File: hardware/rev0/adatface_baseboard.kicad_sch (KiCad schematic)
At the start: 89 parts, among them J1 Conn_01x06_Male, J2 Conn_02x32_Odd_Even, J3 Conn_02x32_Odd_Even, J4 Connector_USB_C_Receptacle_US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, J5 Connector_USB_C_Receptacle_US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, J6 Conn_01x06_Male, J7 Conn_01x23_Male, J8 Conn_01x01_Male, J9 Conn_01x01_Male, U1 PLR135-T10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

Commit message: Fix bugs in rev0
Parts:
- removed J7: Conn_01x23_Male, Connector_PinHeader_2.54mm:PinHeader_1x23_P2.54mm_Vertical, symbol Connector:Conn_01x23_Male
- added J7: Conn_01x26_Male, Connector_PinHeader_2.54mm:PinHeader_1x26_P2.54mm_Horizontal, symbol Connector:Conn_01x26_Male
- J8, J9: footprint Connector_PinHeader_2.54mm:PinHeader_1x01_P2.54mm_Vertical -> Connector_PinHeader_2.54mm:PinHeader_1x01_P2.54mm_Horizontal
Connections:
- net +3V3: now also J7.2 (Pin_2)
- net GND: now also J7.1 (Pin_1), J7.3 (Pin_3)
- net at J2.8 (Pin_8): now also J7.4 (Pin_4)
- net at J2.26 (Pin_26): now also J7.13 (Pin_13)
- net at J2.28 (Pin_28): now also J7.14 (Pin_14)
- net at J2.30 (Pin_30): now also J7.15 (Pin_15)
- net at J2.32 (Pin_32): now also J7.16 (Pin_16)
- net at J2.34 (Pin_34): now also J7.17 (Pin_17)
- net at J2.36 (Pin_36): now also J7.18 (Pin_18)
- net at J2.38 (Pin_38): now also J7.19 (Pin_19)
- net at J2.40 (Pin_40): now also J7.20 (Pin_20)
- net at J2.42 (Pin_42): now also J7.21 (Pin_21)
- net at J2.44 (Pin_44): now also J7.22 (Pin_22)
- net at J2.10 (Pin_10): now also J7.5 (Pin_5)
- net at J2.46 (Pin_46): now also J7.23 (Pin_23)
- net at J2.48 (Pin_48): now also J7.24 (Pin_24)
- net at J2.50 (Pin_50): now also J7.25 (Pin_25)
- net at J2.52 (Pin_52): now also J7.26 (Pin_26)
- net at J2.12 (Pin_12): now also J7.6 (Pin_6)
- net at J2.14 (Pin_14): now also J7.7 (Pin_7)
- net at J2.16 (Pin_16): now also J7.8 (Pin_8)
- net at J2.18 (Pin_18): now also J7.9 (Pin_9)
- net at J2.20 (Pin_20): now also J7.10 (Pin_10)
- net at J2.22 (Pin_22): now also J7.11 (Pin_11)
- net at J2.24 (Pin_24): now also J7.12 (Pin_12)

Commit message: Fix missing symbol and footprint libraries for toslink
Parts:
- TR1, TR2, TR3, TR4: footprint XDCR_PLT133/T10W -> toslink:PLT133_T10W; symbol PLT133_T10W:PLT133_T10W -> toslink:PLT133_T10W
- U1, U2, U3, U4: footprint PLR135-T10_PLT133-T10W -> toslink:PLR135-T10_PLT133-T10W; symbol PLR135_T10:PLR135-T10 -> toslink:PLR135_T10
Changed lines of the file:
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@@
     (pin "1")
   )
-  (symbol (lib_id "PLT133_T10W:PLT133_T10W") (at 82.55 147.32 0) (unit 1)
+  (symbol (lib_id "toslink:PLT133_T10W") (at 82.55 147.32 0) (unit 1)
     (in_bom yes) (on_board yes) (fields_autoplaced)
     (property "Reference" "TR4" (id 0) (at 82.55 135.7334 0))
     (property "Value" "PLT133_T10W" (id 1) (at 82.55 138.5085 0))
-    (property "Footprint" "XDCR_PLT133/T10W" (id 2) (at 82.55 147.32 0)
+    (property "Footprint" "toslink:PLT133_T10W" (id 2) (at 82.55 147.32 0)
       (effects (font (size 1.27 1.27)) (justify left bottom) hide)
     )
@@
     (pin "2")
   )
-  (symbol (lib_id "PLR135_T10:PLR135-T10") (at 83.82 63.5 0) (unit 1)
+  (symbol (lib_id "toslink:PLR135_T10") (at 83.82 63.5 0) (unit 1)
     (in_bom yes) (on_board yes) (fields_autoplaced)
     (property "Reference" "U2" (id 0) (at 93.8785 62.5915 0)
@@
       (effects (font (size 1.27 1.27)) (justify left))
     )
-    (property "Footprint" "PLR135-T10_PLT133-T10W" (id 2) (at 83.82 63.5 0)
+    (property "Footprint" "toslink:PLR135-T10_PLT133-T10W" (id 2) (at 83.82 63.5 0)
       (effects (font (size 1.27 1.27)) (justify left bottom) hide)
     )
@@
     (pin "1")
   )
-  (symbol (lib_id "PLR135_T10:PLR135-T10") (at 83.82 119.38 0) (unit 1)
+  (symbol (lib_id "toslink:PLR135_T10") (at 83.82 119.38 0) (unit 1)
     (in_bom yes) (on_board yes) (fields_autoplaced)
     (property "Reference" "U3" (id 0) (at 93.8785 118.4715 0)
@@
       (effects (font (size 1.27 1.27)) (justify left))
     )
-    (property "Footprint" "PLR135-T10_PLT133-T10W" (id 2) (at 83.82 119.38 0)
+    (property "Footprint" "toslink:PLR135-T10_PLT133-T10W" (id 2) (at 83.82 119.38 0)
       (effects (font (size 1.27 1.27)) (justify left bottom) hide)
     )
@@
     (pin "1")
   )
-  (symbol (lib_id "PLT133_T10W:PLT133_T10W") (at 82.55 91.44 0) (unit 1)
+  (symbol (lib_id "toslink:PLT133_T10W") (at 82.55 91.44 0) (unit 1)
     (in_bom yes) (on_board yes) (fields_autoplaced)
     (property "Reference" "TR3" (id 0) (at 82.55 79.8534 0))
     (property "Value" "PLT133_T10W" (id 1) (at 82.55 82.6285 0))
-    (property "Footprint" "XDCR_PLT133/T10W" (id 2) (at 82.55 91.44 0)
+    (property "Footprint" "toslink:PLT133_T10W" (id 2) (at 82.55 91.44 0)
       (effects (font (size 1.27 1.27)) (justify left bottom) hide)
     )
@@
     (pin "1")
   )
-  (symbol (lib_id "PLT133_T10W:PLT133_T10W") (at 82.55 35.56 0) (unit 1)
+  (symbol (lib_id "toslink:PLT133_T10W") (at 82.55 35.56 0) (unit 1)
     (in_bom yes) (on_board yes) (fields_autoplaced)
     (property "Reference" "TR2" (id 0) (at 82.55 23.9734 0))
     (property "Value" "PLT133_T10W" (id 1) (at 82.55 26.7485 0))
-    (property "Footprint" "XDCR_PLT133/T10W" (id 2) (at 82.55 35.56 0)
+    (property "Footprint" "toslink:PLT133_T10W" (id 2) (at 82.55 35.56 0)
       (effects (font (size 1.27 1.27)) (justify left bottom) hide)
     )
@@
     (pin "5")
   )
-  (symbol (lib_id "PLR135_T10:PLR135-T10") (at 82.55 232.41 0) (unit 1)
+  (symbol (lib_id "toslink:PLR135_T10") (at 82.55 232.41 0) (unit 1)
     (in_bom yes) (on_board yes) (fields_autoplaced)
     (property "Reference" "U1" (id 0) (at 92.6085 231.5015 0)
@@
       (effects (font (size 1.27 1.27)) (justify left))
     )
-    (property "Footprint" "PLR135-T10_PLT133-T10W" (id 2) (at 82.55 232.41 0)
+    (property "Footprint" "toslink:PLR135-T10_PLT133-T10W" (id 2) (at 82.55 232.41 0)
       (effects (font (size 1.27 1.27)) (justify left bottom) hide)
     )
@@
     (pin "1")
   )
-  (symbol (lib_id "PLT133_T10W:PLT133_T10W") (at 81.28 204.47 0) (unit 1)
+  (symbol (lib_id "toslink:PLT133_T10W") (at 81.28 204.47 0) (unit 1)
     (in_bom yes) (on_board yes) (fields_autoplaced)
     (property "Reference" "TR1" (id 0) (at 81.28 192.8834 0))
     (property "Value" "PLT133_T10W" (id 1) (at 81.28 195.6585 0))
-    (property "Footprint" "XDCR_PLT133/T10W" (id 2) (at 82.55 191.77 0)
+    (property "Footprint" "toslink:PLT133_T10W" (id 2) (at 81.28 204.47 0)
       (effects (font (size 1.27 1.27)) (justify left bottom) hide)
     )
@@
       (effects (font (size 1.27 1.27)) (justify left bottom) hide)
     )
-    (property "MAXIMUM_PACKAGE_HEIGHT" "10.3 mm" (id 4) (at 87.63 194.31 0)
+    (property "MAXIMUM_PACKAGE_HEIGHT" "10.3 mm" (id 4) (at 81.28 204.47 0)
       (effects (font (size 1.27 1.27)) (justify left bottom) hide)
     )
-    (property "MANUFACTURER" "Everlight Electronics" (id 5) (at 81.28 214.63 0)
+    (property "MANUFACTURER" "Everlight Electronics" (id 5) (at 81.28 204.47 0)
       (effects (font (size 1.27 1.27)) (justify left bottom) hide)
     )
@@
       (effects (font (size 1.27 1.27)) (justify left bottom) hide)
     )
-    (property "STANDARD" "Manufacturer Recommendations" (id 7) (at 80.01 215.9 0)
+    (property "STANDARD" "Manufacturer Recommendations" (id 7) (at 81.28 204.47 0)
       (effects (font (size 1.27 1.27)) (justify left bottom) hide)
     )
@@
     (pin "1")
   )
-  (symbol (lib_id "PLR135_T10:PLR135-T10") (at 83.82 175.26 0) (unit 1)
+  (symbol (lib_id "toslink:PLR135_T10") (at 83.82 175.26 0) (unit 1)
     (in_bom yes) (on_board yes) (fields_autoplaced)
     (property "Reference" "U4" (id 0) (at 93.8785 174.3515 0)
@@
       (effects (font (size 1.27 1.27)) (justify left))
     )
-    (property "Footprint" "PLR135-T10_PLT133-T10W" (id 2) (at 83.82 175.26 0)
+    (property "Footprint" "toslink:PLR135-T10_PLT133-T10W" (id 2) (at 83.82 175.26 0)
       (effects (font (size 1.27 1.27)) (justify left bottom) hide)
     )
@@
     )
     (path "/e305be24-ecd4-4f67-94e9-58c892d869c0"
-      (reference "TR1") (unit 1) (value "PLT133_T10W") (footprint "XDCR_PLT133/T10W")
+      (reference "TR1") (unit 1) (value "PLT133_T10W") (footprint "toslink:PLT133_T10W")
     )
     (path "/d307c6e7-be3d-479f-a065-7e94414e36ef"
-      (reference "TR2") (unit 1) (value "PLT133_T10W") (footprint "XDCR_PLT133/T10W")
+      (reference "TR2") (unit 1) (value "PLT133_T10W") (footprint "toslink:PLT133_T10W")
     )
     (path "/b68d2074-2874-4baf-9fc7-73bd2b8e0725"
-      (reference "TR3") (unit 1) (value "PLT133_T10W") (footprint "XDCR_PLT133/T10W")
+      (reference "TR3") (unit 1) (value "PLT133_T10W") (footprint "toslink:PLT133_T10W")
     )
     (path "/100b613e-a6ff-4d41-9825-5ac37f8b1fa0"
-      (reference "TR4") (unit 1) (value "PLT133_T10W") (footprint "XDCR_PLT133/T10W")
+      (reference "TR4") (unit 1) (value "PLT133_T10W") (footprint "toslink:PLT133_T10W")
     )
     (path "/d44226c0-bd8c-4098-ad30-873ebe731ecc"
-      (reference "U1") (unit 1) (value "PLR135-T10") (footprint "PLR135-T10_PLT133-T10W")
+      (reference "U1") (unit 1) (value "PLR135-T10") (footprint "toslink:PLR135-T10_PLT133-T10W")
     )
     (path "/99f4d10a-336e-460f-ac98-498fefdb9e43"
-      (reference "U2") (unit 1) (value "PLR135-T10") (footprint "PLR135-T10_PLT133-T10W")
+      (reference "U2") (unit 1) (value "PLR135-T10") (footprint "toslink:PLR135-T10_PLT133-T10W")
     )
     (path "/a504528d-b263-479b-914d-740c72f5070c"
-      (reference "U3") (unit 1) (value "PLR135-T10") (footprint "PLR135-T10_PLT133-T10W")
+      (reference "U3") (unit 1) (value "PLR135-T10") (footprint "toslink:PLR135-T10_PLT133-T10W")
     )
     (path "/e97ce483-a060-4946-827f-bc98193607f2"
-      (reference "U4") (unit 1) (value "PLR135-T10") (footprint "PLR135-T10_PLT133-T10W")
+      (reference "U4") (unit 1) (value "PLR135-T10") (footprint "toslink:PLR135-T10_PLT133-T10W")
     )
     (path "/0b1e87ea-f6ed-4224-97ad-09fa0b4bc814"

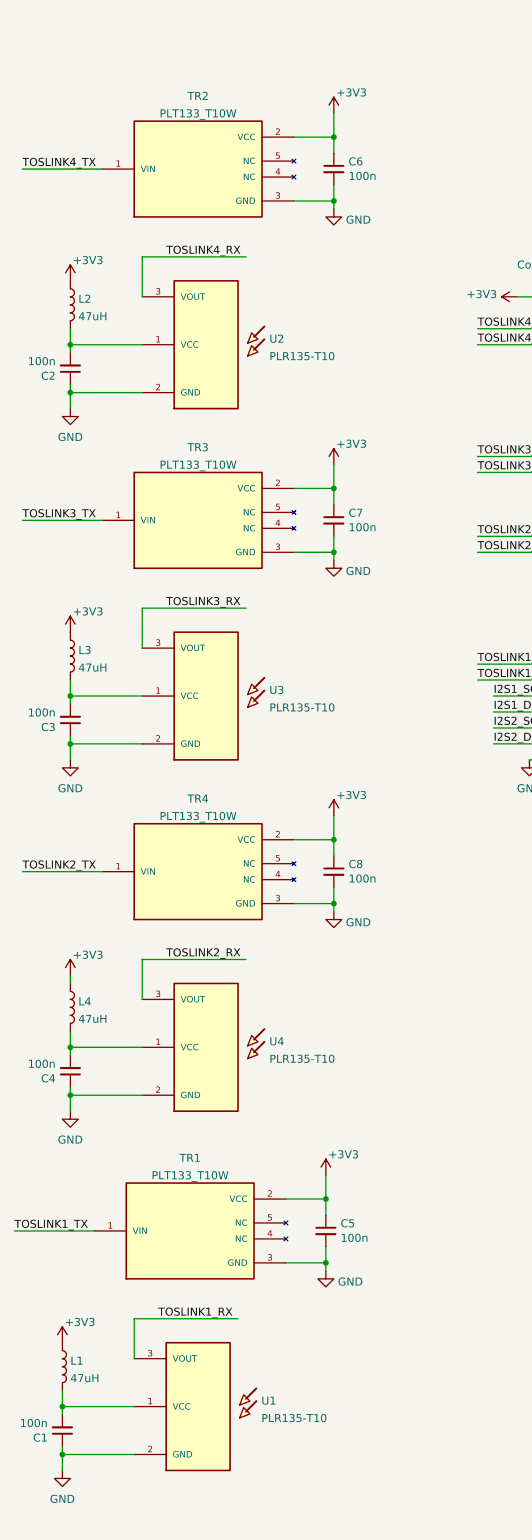
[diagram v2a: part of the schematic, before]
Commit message: change toslink footprints to T8 variation
Footprint is the same except for the edition of NPTH for
plastic mounting feet, so either T8 or T10 versions can
be used.
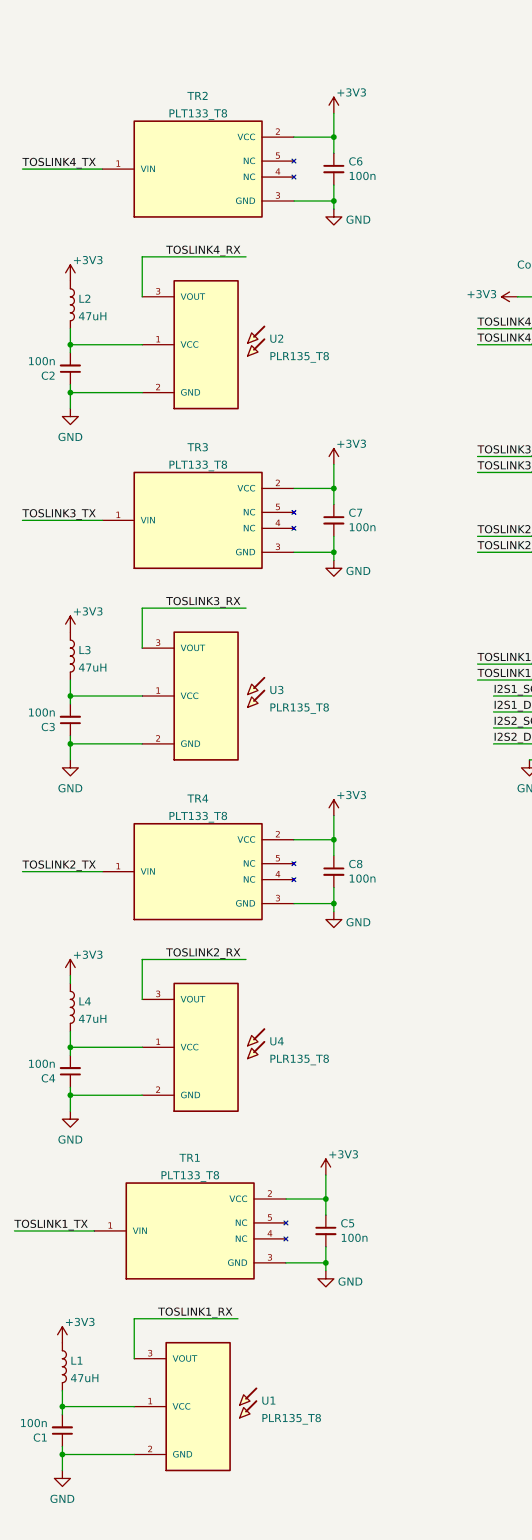
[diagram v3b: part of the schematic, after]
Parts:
- TR1, TR2, TR3, TR4: value PLT133_T10W -> PLT133_T8; footprint toslink:PLT133_T10W -> toslink:PLT133_T8; symbol toslink:PLT133_T10W -> toslink:PLT133_T8
- U1, U2, U3, U4: value PLR135-T10 -> PLR135_T8; footprint toslink:PLR135-T10_PLT133-T10W -> toslink:PLR135-T8_PLT133-T8; symbol toslink:PLR135_T10 -> toslink:PLR135_T8
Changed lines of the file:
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@@
     (pin "1")
   )
-  (symbol (lib_id "toslink:PLT133_T10W") (at 82.55 147.32 0) (unit 1)
+  (symbol (lib_id "toslink:PLT133_T8") (at 82.55 147.32 0) (unit 1)
     (in_bom yes) (on_board yes) (fields_autoplaced)
     (property "Reference" "TR4" (id 0) (at 82.55 135.7334 0))
-    (property "Value" "PLT133_T10W" (id 1) (at 82.55 138.5085 0))
-    (property "Footprint" "toslink:PLT133_T10W" (id 2) (at 82.55 147.32 0)
+    (property "Value" "PLT133_T8" (id 1) (at 82.55 138.5085 0))
+    (property "Footprint" "toslink:PLT133_T8" (id 2) (at 82.55 147.32 0)
       (effects (font (size 1.27 1.27)) (justify left bottom) hide)
     )
@@
     (pin "2")
   )
-  (symbol (lib_id "toslink:PLR135_T10") (at 83.82 63.5 0) (unit 1)
+  (symbol (lib_id "toslink:PLR135_T8") (at 83.82 63.5 0) (unit 1)
     (in_bom yes) (on_board yes) (fields_autoplaced)
     (property "Reference" "U2" (id 0) (at 93.8785 62.5915 0)
       (effects (font (size 1.27 1.27)) (justify left))
     )
-    (property "Value" "PLR135-T10" (id 1) (at 93.8785 65.3666 0)
+    (property "Value" "PLR135_T8" (id 1) (at 93.8785 65.3666 0)
       (effects (font (size 1.27 1.27)) (justify left))
     )
-    (property "Footprint" "toslink:PLR135-T10_PLT133-T10W" (id 2) (at 83.82 63.5 0)
+    (property "Footprint" "toslink:PLR135-T8_PLT133-T8" (id 2) (at 83.82 63.5 0)
       (effects (font (size 1.27 1.27)) (justify left bottom) hide)
     )
@@
     (pin "1")
   )
-  (symbol (lib_id "toslink:PLR135_T10") (at 83.82 119.38 0) (unit 1)
+  (symbol (lib_id "toslink:PLR135_T8") (at 83.82 119.38 0) (unit 1)
     (in_bom yes) (on_board yes) (fields_autoplaced)
     (property "Reference" "U3" (id 0) (at 93.8785 118.4715 0)
       (effects (font (size 1.27 1.27)) (justify left))
     )
-    (property "Value" "PLR135-T10" (id 1) (at 93.8785 121.2466 0)
+    (property "Value" "PLR135_T8" (id 1) (at 93.8785 121.2466 0)
       (effects (font (size 1.27 1.27)) (justify left))
     )
-    (property "Footprint" "toslink:PLR135-T10_PLT133-T10W" (id 2) (at 83.82 119.38 0)
+    (property "Footprint" "toslink:PLR135-T8_PLT133-T8" (id 2) (at 83.82 119.38 0)
       (effects (font (size 1.27 1.27)) (justify left bottom) hide)
     )
@@
     (pin "1")
   )
-  (symbol (lib_id "toslink:PLT133_T10W") (at 82.55 91.44 0) (unit 1)
+  (symbol (lib_id "toslink:PLT133_T8") (at 82.55 91.44 0) (unit 1)
     (in_bom yes) (on_board yes) (fields_autoplaced)
     (property "Reference" "TR3" (id 0) (at 82.55 79.8534 0))
-    (property "Value" "PLT133_T10W" (id 1) (at 82.55 82.6285 0))
-    (property "Footprint" "toslink:PLT133_T10W" (id 2) (at 82.55 91.44 0)
+    (property "Value" "PLT133_T8" (id 1) (at 82.55 82.6285 0))
+    (property "Footprint" "toslink:PLT133_T8" (id 2) (at 82.55 91.44 0)
       (effects (font (size 1.27 1.27)) (justify left bottom) hide)
     )
@@
     (pin "1")
   )
-  (symbol (lib_id "toslink:PLT133_T10W") (at 82.55 35.56 0) (unit 1)
+  (symbol (lib_id "toslink:PLT133_T8") (at 82.55 35.56 0) (unit 1)
     (in_bom yes) (on_board yes) (fields_autoplaced)
     (property "Reference" "TR2" (id 0) (at 82.55 23.9734 0))
-    (property "Value" "PLT133_T10W" (id 1) (at 82.55 26.7485 0))
-    (property "Footprint" "toslink:PLT133_T10W" (id 2) (at 82.55 35.56 0)
+    (property "Value" "PLT133_T8" (id 1) (at 82.55 26.7485 0))
+    (property "Footprint" "toslink:PLT133_T8" (id 2) (at 82.55 35.56 0)
       (effects (font (size 1.27 1.27)) (justify left bottom) hide)
     )
@@
     (pin "5")
   )
-  (symbol (lib_id "toslink:PLR135_T10") (at 82.55 232.41 0) (unit 1)
+  (symbol (lib_id "toslink:PLR135_T8") (at 82.55 232.41 0) (unit 1)
     (in_bom yes) (on_board yes) (fields_autoplaced)
     (property "Reference" "U1" (id 0) (at 92.6085 231.5015 0)
       (effects (font (size 1.27 1.27)) (justify left))
     )
-    (property "Value" "PLR135-T10" (id 1) (at 92.6085 234.2766 0)
+    (property "Value" "PLR135_T8" (id 1) (at 92.6085 234.2766 0)
       (effects (font (size 1.27 1.27)) (justify left))
     )
-    (property "Footprint" "toslink:PLR135-T10_PLT133-T10W" (id 2) (at 82.55 232.41 0)
+    (property "Footprint" "toslink:PLR135-T8_PLT133-T8" (id 2) (at 82.55 232.41 0)
       (effects (font (size 1.27 1.27)) (justify left bottom) hide)
     )
@@
     (pin "1")
   )
-  (symbol (lib_id "toslink:PLT133_T10W") (at 81.28 204.47 0) (unit 1)
+  (symbol (lib_id "toslink:PLT133_T8") (at 81.28 204.47 0) (unit 1)
     (in_bom yes) (on_board yes) (fields_autoplaced)
     (property "Reference" "TR1" (id 0) (at 81.28 192.8834 0))
-    (property "Value" "PLT133_T10W" (id 1) (at 81.28 195.6585 0))
-    (property "Footprint" "toslink:PLT133_T10W" (id 2) (at 81.28 204.47 0)
+    (property "Value" "PLT133_T8" (id 1) (at 81.28 195.6585 0))
+    (property "Footprint" "toslink:PLT133_T8" (id 2) (at 81.28 204.47 0)
       (effects (font (size 1.27 1.27)) (justify left bottom) hide)
     )
@@
     (pin "1")
   )
-  (symbol (lib_id "toslink:PLR135_T10") (at 83.82 175.26 0) (unit 1)
+  (symbol (lib_id "toslink:PLR135_T8") (at 83.82 175.26 0) (unit 1)
     (in_bom yes) (on_board yes) (fields_autoplaced)
     (property "Reference" "U4" (id 0) (at 93.8785 174.3515 0)
       (effects (font (size 1.27 1.27)) (justify left))
     )
-    (property "Value" "PLR135-T10" (id 1) (at 93.8785 177.1266 0)
+    (property "Value" "PLR135_T8" (id 1) (at 93.8785 177.1266 0)
       (effects (font (size 1.27 1.27)) (justify left))
     )
-    (property "Footprint" "toslink:PLR135-T10_PLT133-T10W" (id 2) (at 83.82 175.26 0)
+    (property "Footprint" "toslink:PLR135-T8_PLT133-T8" (id 2) (at 83.82 175.26 0)
       (effects (font (size 1.27 1.27)) (justify left bottom) hide)
     )
@@
     )
     (path "/e305be24-ecd4-4f67-94e9-58c892d869c0"
-      (reference "TR1") (unit 1) (value "PLT133_T10W") (footprint "toslink:PLT133_T10W")
+      (reference "TR1") (unit 1) (value "PLT133_T8") (footprint "toslink:PLT133_T8")
     )
     (path "/d307c6e7-be3d-479f-a065-7e94414e36ef"
-      (reference "TR2") (unit 1) (value "PLT133_T10W") (footprint "toslink:PLT133_T10W")
+      (reference "TR2") (unit 1) (value "PLT133_T8") (footprint "toslink:PLT133_T8")
     )
     (path "/b68d2074-2874-4baf-9fc7-73bd2b8e0725"
-      (reference "TR3") (unit 1) (value "PLT133_T10W") (footprint "toslink:PLT133_T10W")
+      (reference "TR3") (unit 1) (value "PLT133_T8") (footprint "toslink:PLT133_T8")
     )
     (path "/100b613e-a6ff-4d41-9825-5ac37f8b1fa0"
-      (reference "TR4") (unit 1) (value "PLT133_T10W") (footprint "toslink:PLT133_T10W")
+      (reference "TR4") (unit 1) (value "PLT133_T8") (footprint "toslink:PLT133_T8")
     )
     (path "/d44226c0-bd8c-4098-ad30-873ebe731ecc"
-      (reference "U1") (unit 1) (value "PLR135-T10") (footprint "toslink:PLR135-T10_PLT133-T10W")
+      (reference "U1") (unit 1) (value "PLR135_T8") (footprint "toslink:PLR135-T8_PLT133-T8")
     )
     (path "/99f4d10a-336e-460f-ac98-498fefdb9e43"
-      (reference "U2") (unit 1) (value "PLR135-T10") (footprint "toslink:PLR135-T10_PLT133-T10W")
+      (reference "U2") (unit 1) (value "PLR135_T8") (footprint "toslink:PLR135-T8_PLT133-T8")
     )
     (path "/a504528d-b263-479b-914d-740c72f5070c"
-      (reference "U3") (unit 1) (value "PLR135-T10") (footprint "toslink:PLR135-T10_PLT133-T10W")
+      (reference "U3") (unit 1) (value "PLR135_T8") (footprint "toslink:PLR135-T8_PLT133-T8")
     )
     (path "/e97ce483-a060-4946-827f-bc98193607f2"
-      (reference "U4") (unit 1) (value "PLR135-T10") (footprint "toslink:PLR135-T10_PLT133-T10W")
+      (reference "U4") (unit 1) (value "PLR135_T8") (footprint "toslink:PLR135-T8_PLT133-T8")
     )
     (path "/0b1e87ea-f6ed-4224-97ad-09fa0b4bc814"
